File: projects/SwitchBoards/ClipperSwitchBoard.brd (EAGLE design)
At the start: 18.7 x 14.6 mm, 9 parts

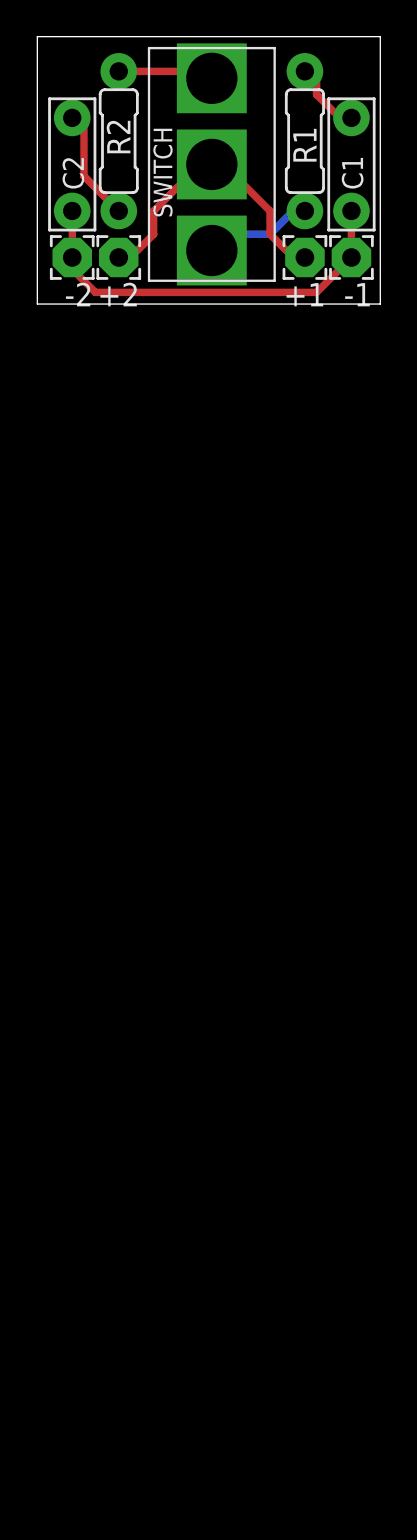
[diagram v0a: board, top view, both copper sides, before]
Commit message: Added clipper boards, filter board update.
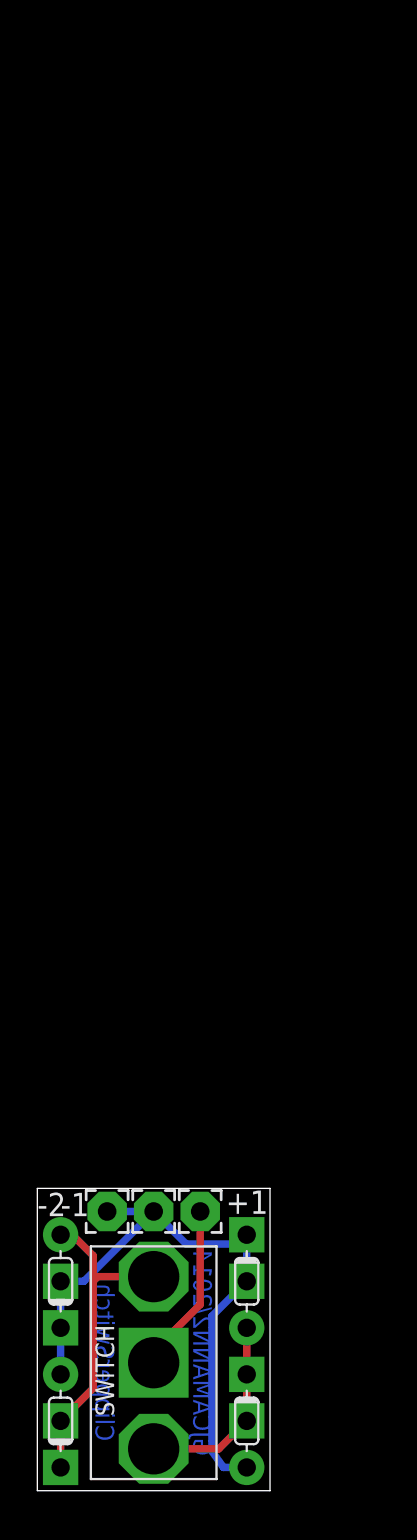
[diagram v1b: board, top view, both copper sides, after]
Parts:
- removed +2: (no value), wirepad:2,15/1,0
- removed C1, C2: (no value), capacitors-film:BOX_SMALL
- removed R1, R2: (no value), resistors:R0207/3
- added U$2, U$3, U$4, U$5: CLIPPER_BLOCK, gc_pedal_parts:CLIPPER_BLOCK
- moved U$1 65.5 mm to (6.35, 6.99)
- moved -1 53.2 mm to (6.35, 15.2), turned to 0 degrees
- moved +1 52.4 mm to (8.89, 15.2), turned to 0 degrees
- moved -2 52.1 mm to (3.81, 15.2), turned to 0 degrees
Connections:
- removed net N$2: C1.2, R1.2
- removed net N$7: +1.1, +2.1, U$1.P$3
- net N$1: now also +1.1, U$1.P$3; no longer R1.1, U$1.P$1
- net N$3: now also U$1.P$1, U$2.P$1, U$2.P$2, U$3.P$3; no longer C2.2, R2.2
- net N$4: now also -1.1, -2.1, U$2.P$3, U$3.P$1, U$3.P$2, U$4.P$3, U$5.P$1, U$5.P$2; no longer R2.1, U$1.P$2
- net N$5: now also U$1.P$2, U$4.P$1, U$4.P$2, U$5.P$3; no longer -1.1, -2.1, C1.1, C2.1
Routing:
- net N$4: track 5.19 -> 35.1 mm
- net N$7: track 15.9 -> 0.00 mm
- net N$2: track 4.34 -> 0.00 mm
- net N$5: track 22.3 -> 18.0 mm
- net N$3: track 6.50 -> 10.8 mm
- net N$1: track 6.06 -> 9.31 mm
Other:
- board size 18.7 x 14.6 mm -> 12.7 x 16.5 mm
- board text added: "ClipperSwitch"
- board text added: "GJCAMANN2/2014"
- board text removed: "FilterSwitchBoard"
- board text removed: "GJCAMANN2014"

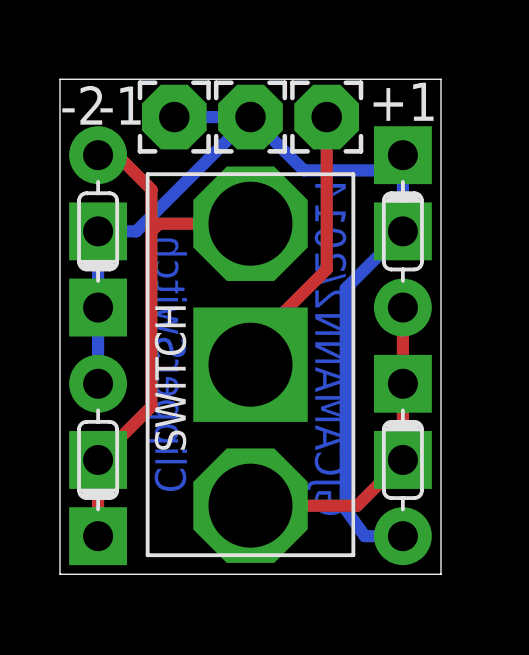
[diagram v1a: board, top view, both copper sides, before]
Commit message: Pass OSHPark DRC.
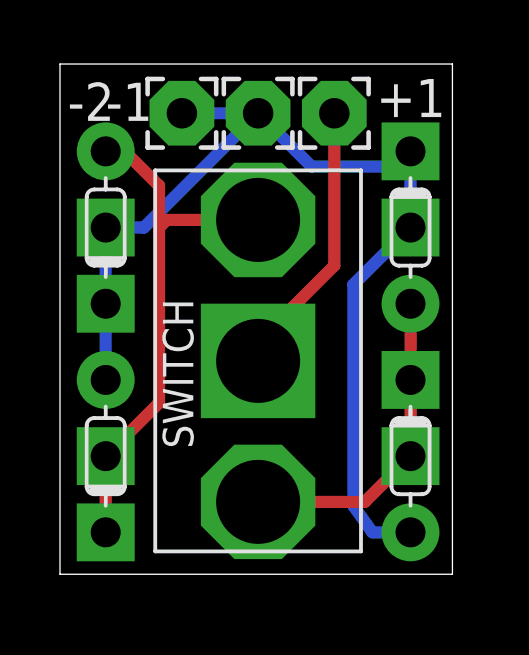
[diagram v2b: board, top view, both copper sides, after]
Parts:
- moved -1 0.28 mm to (6.60, 15.4)
- moved -2 0.28 mm to (4.06, 15.4)
- moved U$1 0.28 mm to (6.60, 7.11)
- moved U$5 0.28 mm to (1.52, 11.6)
- moved +1 0.28 mm to (9.14, 15.4)
- moved U$3 0.28 mm to (11.7, 11.6)
- moved U$4 0.28 mm to (1.52, 3.94)
- moved U$2 0.28 mm to (11.7, 3.94)
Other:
- board size 12.7 x 16.5 mm -> 13.1 x 17 mm

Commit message: Final project updates. Ready to send to oshpark.
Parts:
- moved +1 0.25 mm to (9.14, 15.1)
- moved -1 0.25 mm to (6.60, 15.1)
- moved -2 0.25 mm to (4.06, 15.1)
- turned U$4 to 90 degrees
- turned U$5 to 90 degrees
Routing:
- net N$4: track 35.1 -> 41.9 mm
- net N$5: track 18.0 -> 11.3 mm
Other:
- board text added: "GJCAMANN(C)2014"
- board text added: "V1.0"
- board text removed: "GJCAMANN2/2014"
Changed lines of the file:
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@@
 <wire x1="0" y1="17.008" x2="0" y2="0" width="0" layer="20"/>
 <text x="4.445" y="11.43" size="1.016" layer="22" rot="MR270">ClipperSwitch</text>
-<text x="9.779" y="13.335" size="1.016" layer="22" rot="MR270">GJCAMANN2/2014</text>
+<text x="9.779" y="13.335" size="1.016" layer="22" rot="MR270">GJCAMANN(C)2014</text>
+<text x="2.54" y="1.27" size="0.8128" layer="22" rot="MR180">V1.0</text>
+<wire x1="3.048" y1="12.7" x2="4.445" y2="12.7" width="0.4064" layer="21"/>
+<wire x1="3.937" y1="13.208" x2="4.445" y2="12.7" width="0.4064" layer="21"/>
+<wire x1="4.445" y1="12.7" x2="3.937" y2="12.192" width="0.4064" layer="21"/>
+<wire x1="10.414" y1="2.54" x2="9.017" y2="2.54" width="0.4064" layer="21"/>
+<wire x1="9.525" y1="3.048" x2="9.017" y2="2.54" width="0.4064" layer="21"/>
+<wire x1="9.017" y1="2.54" x2="9.525" y2="2.032" width="0.4064" layer="21"/>
+<wire x1="7.747" y1="16.256" x2="7.493" y2="16.51" width="0.4064" layer="21"/>
+<wire x1="7.493" y1="16.51" x2="3.175" y2="16.51" width="0.4064" layer="21"/>
+<wire x1="3.175" y1="16.51" x2="2.921" y2="16.256" width="0.4064" layer="21"/>
 </plain>
 <attributes>
@@
 <element name="U$2" library="gc_pedal_parts" package="CLIPPER_BLOCK" value="CLIPPER_BLOCK" x="11.684" y="3.937" rot="R90"/>
 <element name="U$3" library="gc_pedal_parts" package="CLIPPER_BLOCK" value="CLIPPER_BLOCK" x="11.684" y="11.557" rot="R90"/>
-<element name="U$4" library="gc_pedal_parts" package="CLIPPER_BLOCK" value="CLIPPER_BLOCK" x="1.524" y="3.937" rot="R270"/>
-<element name="U$5" library="gc_pedal_parts" package="CLIPPER_BLOCK" value="CLIPPER_BLOCK" x="1.524" y="11.557" rot="R270"/>
-<element name="+1" library="wirepad" package="2,15/1,0" value="" x="9.144" y="15.367" smashed="yes">
-<attribute name="NAME" x="10.541" y="15.24" size="1.27" layer="25" ratio="10"/>
-<attribute name="VALUE" x="9.144" y="16.367" size="0.0254" layer="27"/>
+<element name="U$4" library="gc_pedal_parts" package="CLIPPER_BLOCK" value="CLIPPER_BLOCK" x="1.524" y="3.937" rot="R90"/>
+<element name="U$5" library="gc_pedal_parts" package="CLIPPER_BLOCK" value="CLIPPER_BLOCK" x="1.524" y="11.557" rot="R90"/>
+<element name="+1" library="wirepad" package="2,15/1,0" value="" x="9.144" y="15.113" smashed="yes">
+<attribute name="NAME" x="10.541" y="14.986" size="1.27" layer="25" ratio="10"/>
+<attribute name="VALUE" x="9.144" y="16.113" size="0.0254" layer="27"/>
 </element>
-<element name="-2" library="wirepad" package="2,15/1,0" value="" x="4.064" y="15.367" smashed="yes">
-<attribute name="NAME" x="0.254" y="15.113" size="1.27" layer="25" ratio="10"/>
-<attribute name="VALUE" x="4.064" y="16.367" size="0.0254" layer="27"/>
+<element name="-2" library="wirepad" package="2,15/1,0" value="" x="4.064" y="15.113" smashed="yes">
+<attribute name="NAME" x="0.254" y="14.859" size="1.27" layer="25" ratio="10"/>
+<attribute name="VALUE" x="4.064" y="16.113" size="0.0254" layer="27"/>
 </element>
-<element name="-1" library="wirepad" package="2,15/1,0" value="" x="6.604" y="15.367" smashed="yes">
-<attribute name="NAME" x="1.524" y="15.113" size="1.27" layer="25" ratio="10"/>
-<attribute name="VALUE" x="6.604" y="16.367" size="0.0254" layer="27"/>
+<element name="-1" library="wirepad" package="2,15/1,0" value="" x="6.604" y="15.113" smashed="yes">
+<attribute name="NAME" x="1.524" y="14.859" size="1.27" layer="25" ratio="10"/>
+<attribute name="VALUE" x="6.604" y="16.113" size="0.0254" layer="27"/>
 </element>
 </elements>
@@
 <wire x1="6.604" y1="7.112" x2="6.604" y2="7.747" width="0.4064" layer="1"/>
 <wire x1="6.604" y1="7.747" x2="9.144" y2="10.287" width="0.4064" layer="1"/>
-<wire x1="9.144" y1="10.287" x2="9.144" y2="15.367" width="0.4064" layer="1"/>
+<wire x1="9.144" y1="10.287" x2="9.144" y2="15.113" width="0.4064" layer="1"/>
 </signal>
 <signal name="N$3">
@@
 <contactref element="-2" pad="1"/>
 <contactref element="-1" pad="1"/>
-<wire x1="1.524" y1="6.477" x2="1.524" y2="9.017" width="0.4064" layer="16"/>
-<wire x1="1.524" y1="9.017" x2="1.524" y2="11.557" width="0.4064" layer="16"/>
-<wire x1="1.524" y1="11.557" x2="2.794" y2="11.557" width="0.4064" layer="16"/>
-<wire x1="2.794" y1="11.557" x2="6.604" y2="15.367" width="0.4064" layer="16"/>
 <wire x1="11.684" y1="11.557" x2="11.684" y2="13.589" width="0.4064" layer="16"/>
 <wire x1="11.684" y1="13.589" x2="11.684" y2="14.097" width="0.4064" layer="16"/>
@@
 <wire x1="9.779" y1="2.286" x2="9.779" y2="9.652" width="0.4064" layer="16"/>
 <wire x1="9.779" y1="9.652" x2="11.684" y2="11.557" width="0.4064" layer="16"/>
-<wire x1="4.064" y1="15.367" x2="6.604" y2="15.367" width="0.4064" layer="16"/>
-<wire x1="6.604" y1="15.367" x2="8.382" y2="13.589" width="0.4064" layer="16"/>
+<wire x1="4.064" y1="15.113" x2="6.604" y2="15.113" width="0.4064" layer="16"/>
+<wire x1="6.604" y1="15.113" x2="8.382" y2="13.589" width="0.4064" layer="16"/>
 <wire x1="8.382" y1="13.589" x2="11.684" y2="13.589" width="0.4064" layer="16"/>
+<wire x1="1.524" y1="14.097" x2="1.524" y2="11.557" width="0.4064" layer="16"/>
+<wire x1="1.524" y1="1.397" x2="2.667" y2="1.397" width="0.4064" layer="16"/>
+<wire x1="2.667" y1="1.397" x2="3.81" y2="2.54" width="0.4064" layer="16"/>
+<wire x1="3.81" y1="2.54" x2="3.81" y2="10.16" width="0.4064" layer="16"/>
+<wire x1="3.81" y1="10.16" x2="2.54" y2="11.43" width="0.4064" layer="16"/>
+<wire x1="2.54" y1="11.43" x2="1.651" y2="11.43" width="0.4064" layer="16"/>
+<wire x1="1.651" y1="11.43" x2="1.524" y2="11.557" width="0.4064" layer="16"/>
+<wire x1="1.524" y1="14.097" x2="2.54" y2="15.113" width="0.4064" layer="16"/>
+<wire x1="2.54" y1="15.113" x2="4.064" y2="15.113" width="0.4064" layer="16"/>
 </signal>
 <signal name="N$5">
@@
 <contactref element="U$5" pad="P$3"/>
 <contactref element="U$1" pad="P$2"/>
-<wire x1="1.524" y1="14.097" x2="2.159" y2="14.097" width="0.4064" layer="1"/>
-<wire x1="2.159" y1="14.097" x2="3.302" y2="12.954" width="0.4064" layer="1"/>
-<wire x1="3.302" y1="12.954" x2="3.302" y2="11.557" width="0.4064" layer="1"/>
-<wire x1="3.302" y1="11.557" x2="3.302" y2="5.715" width="0.4064" layer="1"/>
-<wire x1="3.302" y1="5.715" x2="1.524" y2="3.937" width="0.4064" layer="1"/>
-<wire x1="1.524" y1="3.937" x2="1.524" y2="1.397" width="0.4064" layer="1"/>
-<wire x1="6.604" y1="11.811" x2="3.556" y2="11.811" width="0.4064" layer="1"/>
-<wire x1="3.556" y1="11.811" x2="3.302" y2="11.557" width="0.4064" layer="1"/>
+<wire x1="1.524" y1="3.937" x2="1.524" y2="6.477" width="0.4064" layer="1"/>
+<wire x1="1.524" y1="6.477" x2="1.524" y2="9.017" width="0.4064" layer="1"/>
+<wire x1="1.524" y1="9.017" x2="2.667" y2="9.017" width="0.4064" layer="1"/>
+<wire x1="2.667" y1="9.017" x2="5.08" y2="11.43" width="0.4064" layer="1"/>
+<wire x1="5.08" y1="11.43" x2="6.223" y2="11.43" width="0.4064" layer="1"/>
+<wire x1="6.223" y1="11.43" x2="6.604" y2="11.811" width="0.4064" layer="1"/>
 </signal>
 </signals>
